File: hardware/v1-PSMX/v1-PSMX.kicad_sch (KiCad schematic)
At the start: 36 parts, among them IC1 MAX98357AETE+T (L), IC2 MAX98357AETE+T (R), J1 +5v_POWER, J2 Conn_01x04, J3 10118192-0002LF, J4 Serial_Breakout, U1 ESP32-S3-WROOM-1, U2 AZ1084-3.3

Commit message: all routed, but needs organized
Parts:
- J4: footprint Connector_PinHeader_2.54mm:PinHeader_1x06_P2.54mm_Vertical -> Connector_PinHeader_2.54mm:PinHeader_2x02_P2.54mm_Vertical; symbol Connector_Generic:Conn_01x06 -> Connector_Generic:Conn_01x04
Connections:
- net RESET: no longer J4.4 (Pin_4)
- net RST_TO_PRGM: no longer J4.3 (Pin_3)
- net U0RXD_TX: now also J4.3 (Pin_3); no longer J4.5 (Pin_5)
- net U0TXD_RX: now also J4.4 (Pin_4); no longer J4.6 (Pin_6)
- net V_POT_GPIO09: now also C9.1, VR2.2 (WIPER); no longer C8.1, VR1.2 (WIPER)
- net S_POT_GPIO02: now reaches U1.38 (GPIO2/TOUCH2/ADC1_CH1)
- net S_POT_GPIO02: now also C8.1, VR1.2 (WIPER)
- removed net S_POT_GPIO10: C9.1, U1.18 (GPIO10/TOUCH10/ADC1_CH9/FSPICS0/FSPIIO4/SUBSPICS0), VR2.2 (WIPER)
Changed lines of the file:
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@@
   (no_connect (at 195.326 53.594))
   (no_connect (at 195.326 81.534))
+  (no_connect (at 81.026 66.294))
   (no_connect (at 236.474 40.132))
   (no_connect (at 195.326 61.214))
@@
   (no_connect (at 195.326 51.054))
   (no_connect (at 195.326 56.134))
-  (no_connect (at 81.026 45.974))
   (no_connect (at 139.7 164.338))
   (no_connect (at 81.026 81.534))
@@
     (stroke (width 0) (type default) (color 0 0 0 0))
   )
-  (wire (pts (xy 238.506 81.026) (xy 239.522 81.026))
+  (wire (pts (xy 238.506 84.836) (xy 239.522 84.836))
     (stroke (width 0) (type default) (color 0 0 0 0))
   )
@@
     (stroke (width 0) (type default) (color 0 0 0 0))
   )
-  (wire (pts (xy 237.49 83.566) (xy 239.522 83.566))
-    (stroke (width 0) (type default) (color 0 0 0 0))
-  )
   (wire (pts (xy 231.902 37.592) (xy 236.474 37.592))
     (stroke (width 0) (type default) (color 0 0 0 0))
@@
     (stroke (width 0) (type default) (color 0 0 0 0))
   )
-  (wire (pts (xy 238.506 80.01) (xy 238.506 81.026))
+  (wire (pts (xy 238.506 83.82) (xy 238.506 84.836))
     (stroke (width 0) (type default) (color 0 0 0 0))
   )
@@
     (stroke (width 0) (type default) (color 0 0 0 0))
   )
-  (wire (pts (xy 238.506 78.486) (xy 239.522 78.486))
+  (wire (pts (xy 238.506 82.296) (xy 239.522 82.296))
     (stroke (width 0) (type default) (color 0 0 0 0))
   )
@@
     (stroke (width 0) (type default) (color 0 0 0 0))
   )
-  (wire (pts (xy 237.49 86.106) (xy 239.522 86.106))
-    (stroke (width 0) (type default) (color 0 0 0 0))
-  )
   (wire (pts (xy 259.334 110.998) (xy 262.128 110.998))
     (stroke (width 0) (type default) (color 0 0 0 0))
@@
     (stroke (width 0) (type default) (color 0 0 0 0))
   )
-  (wire (pts (xy 78.232 66.294) (xy 81.026 66.294))
+  (wire (pts (xy 78.232 45.974) (xy 81.026 45.974))
     (stroke (width 0) (type default) (color 0 0 0 0))
   )
@@
     (stroke (width 0) (type default) (color 0 0 0 0))
   )
-  (wire (pts (xy 237.49 77.47) (xy 238.506 77.47))
-    (stroke (width 0) (type default) (color 0 0 0 0))
-  )
-  (wire (pts (xy 239.522 91.186) (xy 237.49 91.186))
+  (wire (pts (xy 237.49 81.28) (xy 238.506 81.28))
+    (stroke (width 0) (type default) (color 0 0 0 0))
+  )
+  (wire (pts (xy 239.522 89.916) (xy 237.49 89.916))
     (stroke (width 0) (type default) (color 0 0 0 0))
   )
@@
     (stroke (width 0) (type default) (color 0 0 0 0))
   )
-  (wire (pts (xy 238.506 77.47) (xy 238.506 78.486))
+  (wire (pts (xy 238.506 81.28) (xy 238.506 82.296))
     (stroke (width 0) (type default) (color 0 0 0 0))
   )
@@
     (stroke (width 0) (type default) (color 0 0 0 0))
   )
-  (wire (pts (xy 237.49 80.01) (xy 238.506 80.01))
+  (wire (pts (xy 237.49 83.82) (xy 238.506 83.82))
     (stroke (width 0) (type default) (color 0 0 0 0))
   )
@@
     (stroke (width 0) (type default) (color 0 0 0 0))
   )
-  (wire (pts (xy 239.522 88.646) (xy 237.49 88.646))
+  (wire (pts (xy 239.522 87.376) (xy 237.49 87.376))
     (stroke (width 0) (type default) (color 0 0 0 0))
   )
@@
     (effects (font (size 1.27 1.27) (thickness 0.254) bold) (justify left bottom))
   )
-  (text "RX (MASTER)" (at 246.634 91.186 0)
+  (text "RX (MASTER)" (at 246.634 90.424 0)
     (effects (font (size 1.27 1.27)) (justify left bottom))
   )
-  (text "TX (MASTER)" (at 246.888 88.646 0)
+  (text "TX (MASTER)" (at 246.888 87.884 0)
     (effects (font (size 1.27 1.27)) (justify left bottom))
   )
-  (label "S_POT_GPIO10" (at 198.628 121.92 0)
+  (label "V_POT_GPIO09" (at 198.628 121.92 0)
     (effects (font (size 1.27 1.27)) (justify left bottom))
   )
@@
     (effects (font (size 1.27 1.27)) (justify right bottom))
   )
-  (label "S_POT_GPIO10" (at 78.232 66.294 180)
+  (label "S_POT_GPIO02" (at 78.232 45.974 180)
     (effects (font (size 1.27 1.27)) (justify right bottom))
   )
@@
     (effects (font (size 1.27 1.27)) (justify right bottom))
   )
-  (label "U0TXD_RX" (at 237.49 91.186 180)
+  (label "U0TXD_RX" (at 237.49 89.916 180)
     (effects (font (size 1.27 1.27)) (justify right bottom))
   )
@@
     (effects (font (size 1.27 1.27)) (justify right bottom))
   )
-  (label "RST_TO_PRGM" (at 237.49 83.566 180)
-    (effects (font (size 1.27 1.27)) (justify right bottom))
-  )
   (label "RST_TO_PRGM" (at 51.308 27.94 180)
     (effects (font (size 1.27 1.27)) (justify right bottom))
@@
     (effects (font (size 1.27 1.27)) (justify left bottom))
   )
-  (label "RESET" (at 237.49 86.106 180)
-    (effects (font (size 1.27 1.27)) (justify right bottom))
-  )
-  (label "U0RXD_TX" (at 237.49 88.646 180)
+  (label "U0RXD_TX" (at 237.49 87.376 180)
     (effects (font (size 1.27 1.27)) (justify right bottom))
   )
@@
     (effects (font (size 1.27 1.27)) (justify right bottom))
   )
-  (label "V_POT_GPIO09" (at 170.688 121.412 0)
+  (label "S_POT_GPIO02" (at 170.688 121.412 0)
     (effects (font (size 1.27 1.27)) (justify left bottom))
   )
@@
     (pin "1")
   )
-  (symbol (lib_id "Connector_Generic:Conn_01x06") (at 244.602 83.566 0) (unit 1)
-    (in_bom yes) (on_board yes)
-    (property "Reference" "J4" (id 0) (at 243.586 72.898 0)
-      (effects (font (size 1.27 1.27)) (justify left))
-    )
-    (property "Value" "Serial_Breakout" (id 1) (at 237.236 75.438 0)
-      (effects (font (size 1.27 1.27)) (justify left))
-    )
-    (property "Footprint" "Connector_PinHeader_2.54mm:PinHeader_1x06_P2.54mm_Vertical" (id 2) (at 244.602 83.566 0)
-      (effects (font (size 1.27 1.27)) hide)
-    )
-    (property "Datasheet" "~" (id 3) (at 244.602 83.566 0)
+  (symbol (lib_id "Connector_Generic:Conn_01x04") (at 244.602 84.836 0) (unit 1)
+    (in_bom yes) (on_board yes)
+    (property "Reference" "J4" (id 0) (at 243.586 74.168 0)
+      (effects (font (size 1.27 1.27)) (justify left))
+    )
+    (property "Value" "Serial_Breakout" (id 1) (at 237.236 76.708 0)
+      (effects (font (size 1.27 1.27)) (justify left))
+    )
+    (property "Footprint" "Connector_PinHeader_2.54mm:PinHeader_2x02_P2.54mm_Vertical" (id 2) (at 244.602 84.836 0)
+      (effects (font (size 1.27 1.27)) hide)
+    )
+    (property "Datasheet" "~" (id 3) (at 244.602 84.836 0)
       (effects (font (size 1.27 1.27)) hide)
     )
@@
     (pin "3")
     (pin "4")
-    (pin "5")
-    (pin "6")
   )
   (symbol (lib_id "CLMVC-FKA-CL1D1L71BB7C3C3:CLMVC-FKA-CL1D1L71BB7C3C3") (at 24.765 60.96 90) (unit 1)
@@
     (pin "1")
   )
-  (symbol (lib_id "power:+5V") (at 237.49 77.47 90) (unit 1)
-    (in_bom yes) (on_board yes)
-    (property "Reference" "#PWR032" (id 0) (at 241.3 77.47 0)
-      (effects (font (size 1.27 1.27)) hide)
-    )
-    (property "Value" "+5V" (id 1) (at 231.902 77.47 90))
-    (property "Footprint" "" (id 2) (at 237.49 77.47 0)
-      (effects (font (size 1.27 1.27)) hide)
-    )
-    (property "Datasheet" "" (id 3) (at 237.49 77.47 0)
+  (symbol (lib_id "power:+5V") (at 237.49 81.28 90) (unit 1)
+    (in_bom yes) (on_board yes)
+    (property "Reference" "#PWR032" (id 0) (at 241.3 81.28 0)
+      (effects (font (size 1.27 1.27)) hide)
+    )
+    (property "Value" "+5V" (id 1) (at 231.902 81.28 90))
+    (property "Footprint" "" (id 2) (at 237.49 81.28 0)
+      (effects (font (size 1.27 1.27)) hide)
+    )
+    (property "Datasheet" "" (id 3) (at 237.49 81.28 0)
       (effects (font (size 1.27 1.27)) hide)
     )
@@
     (pin "4")
   )
-  (symbol (lib_id "power:GND") (at 237.49 80.01 270) (unit 1)
-    (in_bom yes) (on_board yes)
-    (property "Reference" "#PWR033" (id 0) (at 231.14 80.01 0)
-      (effects (font (size 1.27 1.27)) hide)
-    )
-    (property "Value" "GND" (id 1) (at 231.902 80.01 90))
-    (property "Footprint" "" (id 2) (at 237.49 80.01 0)
-      (effects (font (size 1.27 1.27)) hide)
-    )
-    (property "Datasheet" "" (id 3) (at 237.49 80.01 0)
+  (symbol (lib_id "power:GND") (at 237.49 83.82 270) (unit 1)
+    (in_bom yes) (on_board yes)
+    (property "Reference" "#PWR033" (id 0) (at 231.14 83.82 0)
+      (effects (font (size 1.27 1.27)) hide)
+    )
+    (property "Value" "GND" (id 1) (at 231.902 83.82 90))
+    (property "Footprint" "" (id 2) (at 237.49 83.82 0)
+      (effects (font (size 1.27 1.27)) hide)
+    )
+    (property "Datasheet" "" (id 3) (at 237.49 83.82 0)
       (effects (font (size 1.27 1.27)) hide)
     )
@@
     )
     (path "/25b181d7-711f-4f0e-870f-5f727244ced0"
-      (reference "J4") (unit 1) (value "Serial_Breakout") (footprint "Connector_PinHeader_2.54mm:PinHeader_1x06_P2.54mm_Vertical")
+      (reference "J4") (unit 1) (value "Serial_Breakout") (footprint "Connector_PinHeader_2.54mm:PinHeader_2x02_P2.54mm_Vertical")
     )
     (path "/2d104990-cbf2-4ea2-be26-2bbd3f2d98d5"

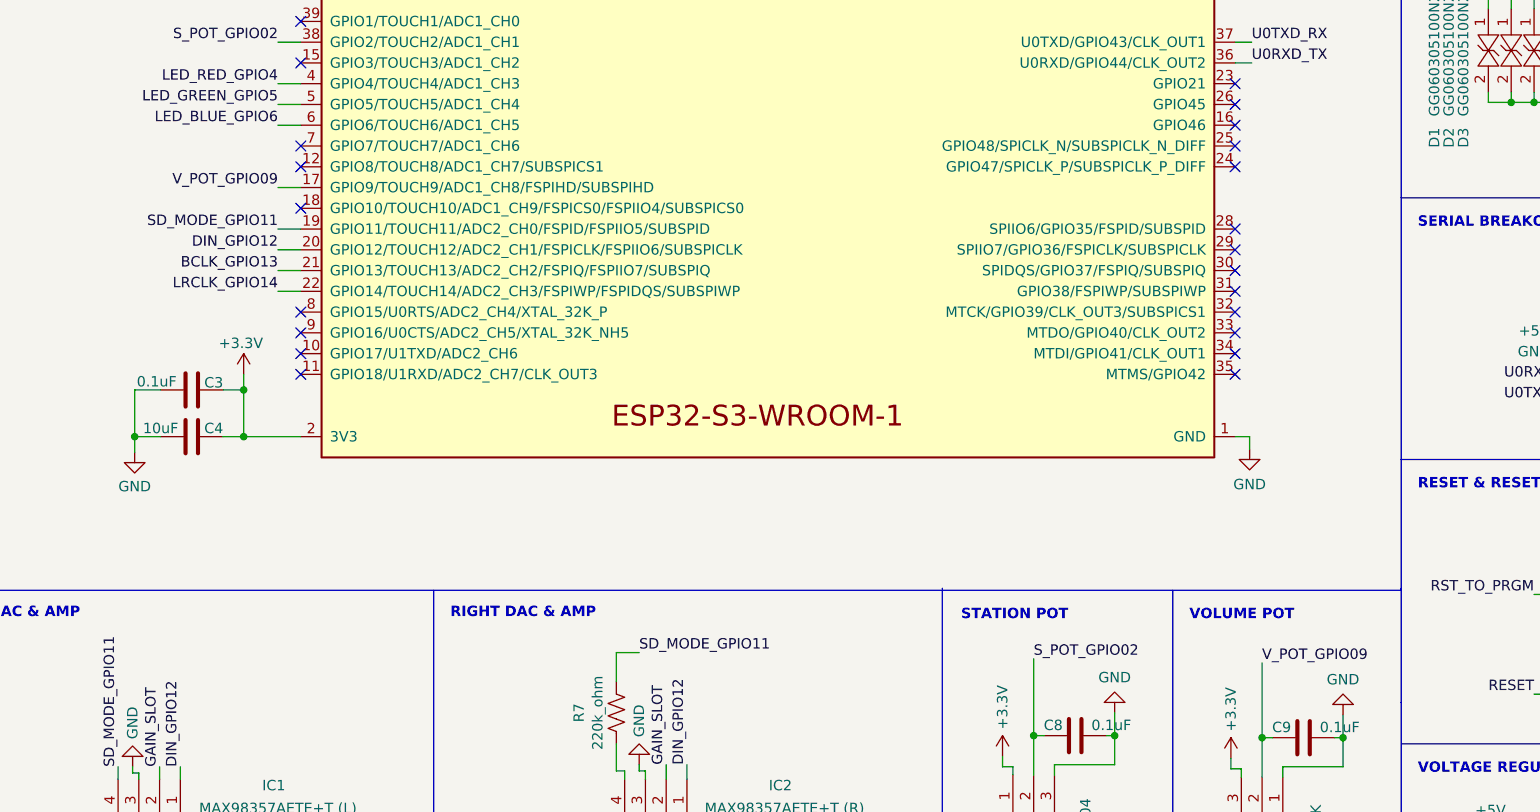
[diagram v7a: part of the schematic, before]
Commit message: Cleaned up pcb
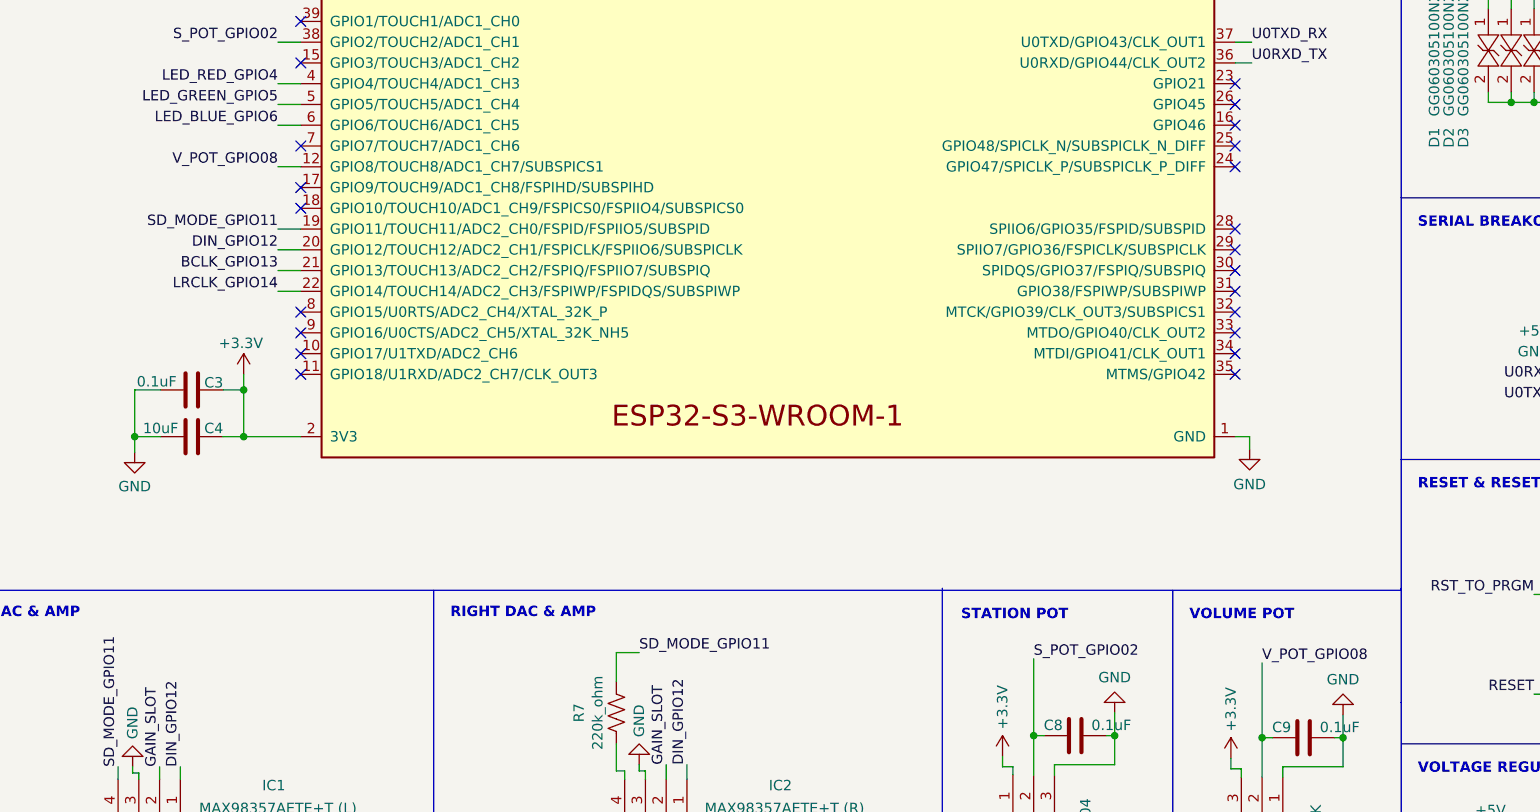
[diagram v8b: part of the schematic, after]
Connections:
- net V_POT_GPIO08: now reaches U1.12 (GPIO8/TOUCH8/ADC1_CH7/SUBSPICS1)
- net V_POT_GPIO08: now also C9.1, VR2.2 (WIPER)
- removed net V_POT_GPIO09: C9.1, U1.17 (GPIO9/TOUCH9/ADC1_CH8/FSPIHD/SUBSPIHD), VR2.2 (WIPER)
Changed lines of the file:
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@@
   (no_connect (at 51.054 157.988))
   (no_connect (at 81.026 84.074))
-  (no_connect (at 81.026 61.214))
+  (no_connect (at 81.026 63.754))
   (no_connect (at 195.326 71.374))
   (no_connect (at 81.026 43.434))
@@
     (stroke (width 0) (type default) (color 0 0 0 0))
   )
-  (wire (pts (xy 78.232 63.754) (xy 81.026 63.754))
+  (wire (pts (xy 78.232 61.214) (xy 81.026 61.214))
     (stroke (width 0) (type default) (color 0 0 0 0))
   )
@@
     (effects (font (size 1.27 1.27)) (justify left bottom))
   )
-  (label "V_POT_GPIO09" (at 198.628 121.92 0)
+  (label "V_POT_GPIO08" (at 198.628 121.92 0)
     (effects (font (size 1.27 1.27)) (justify left bottom))
   )
@@
     (effects (font (size 1.27 1.27)) (justify right bottom))
   )
-  (label "V_POT_GPIO09" (at 78.232 63.754 180)
-    (effects (font (size 1.27 1.27)) (justify right bottom))
-  )
+  (label "V_POT_GPIO08" (at 78.232 61.214 180)
+    (effects (font (size 1.27 1.27)) (justify right bottom))
+  )
